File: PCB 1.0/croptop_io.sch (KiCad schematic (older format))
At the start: 57 parts, among them J5 Terminal Block, J6 DNP, J7 DNP, U10 AD7799, U11 74HCT125D, U17 DT6250-06MR-13, U18 PUSBM5V5X4, U8 74HCT125D, U9 DRV8872

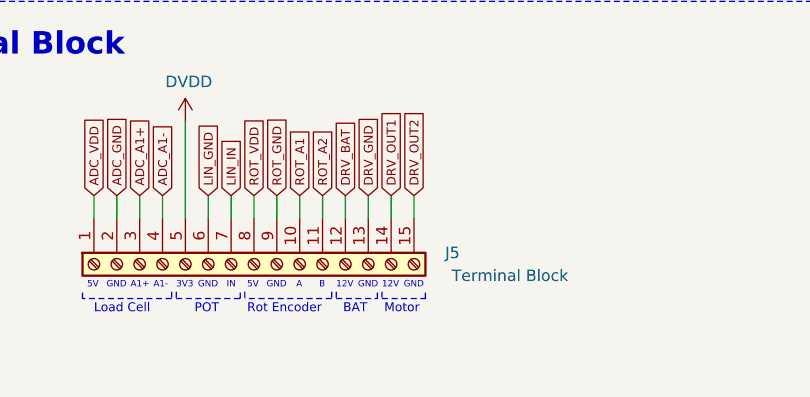
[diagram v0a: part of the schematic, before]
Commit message: New microcontroller pinout
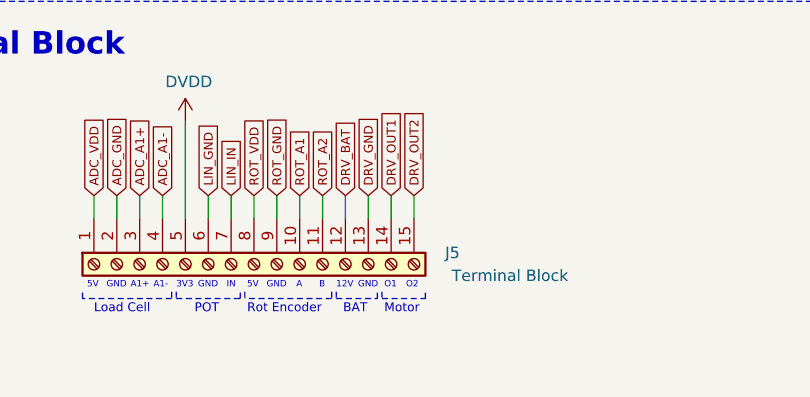
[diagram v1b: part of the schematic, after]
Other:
- note added: "O1"
- note added: "O2\n"
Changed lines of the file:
@@
 Text Notes 3530 7610 0    28   ~ 0
 GND
-Text Notes 3635 7610 0    28   ~ 0
-12V
-Text Notes 3730 7610 0    28   ~ 0
-GND
+Text Notes 3645 7610 0    28   ~ 0
+O1
+Text Notes 3740 7610 0    28   ~ 0
+O2\n
 Wire Notes Line
 	2715 7620 2715 7650
